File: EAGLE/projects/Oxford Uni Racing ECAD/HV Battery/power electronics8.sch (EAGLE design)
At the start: 65 parts, among them IC1 4043D, IC2 SE555D, IC3 4011D, IC6 4011D, K1 T9AS1D12-48=T9A, K2 T9AS5D12-12=T9A, K3 T9AS1D12-48=T9A, K4 T9AS1D12-48=T9A, K5 T9AS1D12-48=T9A, Q1 BSS138, Q2 BSS138, Q3 BSS138, Q4 BSS138, Q5 BSS138

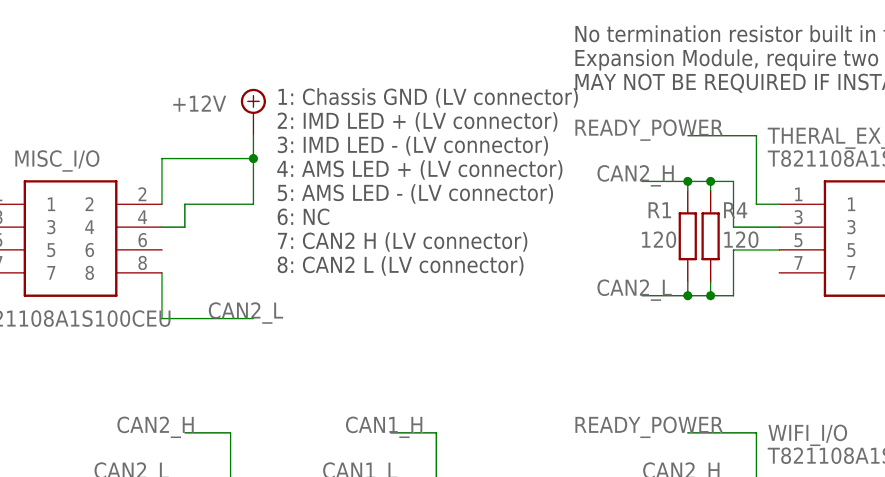
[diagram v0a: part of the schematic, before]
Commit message: connected CAN 1 to misc pcb connector allowing it to be fed to the lv pack connector. This was missing. This has also meant having a single 12V output for both the IMD and AMS warning lights
Signed-off-by: Jack Bruford <jack.bruford41@gmail.com>
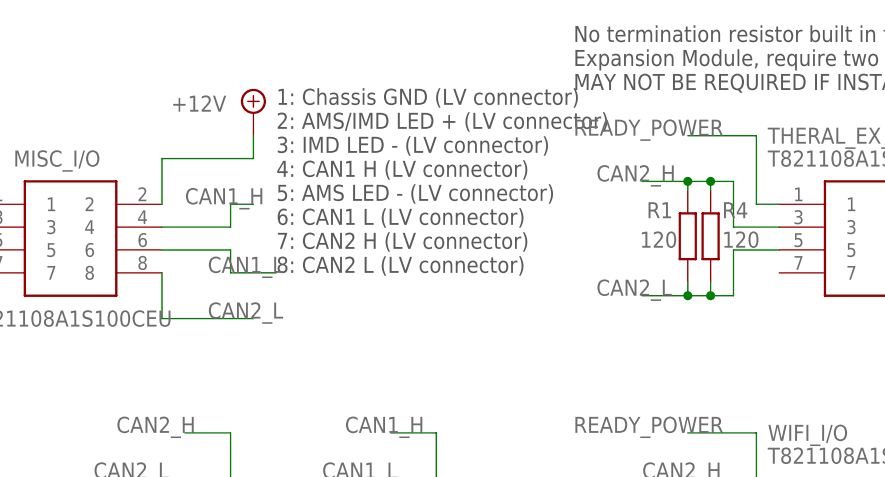
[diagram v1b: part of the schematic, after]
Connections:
- net +12V: no longer MISC_I/O.4
- net CAN1_H: now also MISC_I/O.4
- net CAN1_L: now also MISC_I/O.6
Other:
- note added: "1: Chassis GND (LV connector) 2: AMS/IMD LED + (LV connector) 3: IMD LED - (LV connector) 4: CAN1 H (LV connector) 5: AMS LED - (LV connector) 6: CAN1 L (LV connector) 7: CAN2 H (LV connector) 8: CAN2 L (LV connector)"
- note removed: "1: Chassis GND (LV connector) 2: IMD LED + (LV connector) 3: IMD LED - (LV connector) 4: AMS LED + (LV connector) 5: AMS LED - (LV connector) 6: NC 7: CAN2 H (LV connector) 8: CAN2 L (LV connector)"
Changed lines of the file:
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@@
  a battery voltage source in the application notes</text>
 <text x="170.18" y="152.4" size="1.778" layer="97">1: Chassis GND (LV connector)
-2: IMD LED + (LV connector)
+2: AMS/IMD LED + (LV connector)
 3: IMD LED - (LV connector)
-4: AMS LED + (LV connector)
+4: CAN1 H (LV connector)
 5: AMS LED - (LV connector)
-6: NC
+6: CAN1 L (LV connector)
 7: CAN2 H (LV connector)
 8: CAN2 L (LV connector)</text>
@@
 <pinref part="SUPPLY8" gate="+12V" pin="+12V"/>
 <wire x1="167.64" y1="167.64" x2="167.64" y2="165.1" width="0.1524" layer="91"/>
-<pinref part="MISC_I/O" gate="G$1" pin="4"/>
-<wire x1="157.48" y1="157.48" x2="160.02" y2="157.48" width="0.1524" layer="91"/>
-<wire x1="160.02" y1="157.48" x2="160.02" y2="160.02" width="0.1524" layer="91"/>
-<wire x1="160.02" y1="160.02" x2="167.64" y2="160.02" width="0.1524" layer="91"/>
-<wire x1="167.64" y1="165.1" x2="167.64" y2="160.02" width="0.1524" layer="91"/>
-<junction x="167.64" y="165.1"/>
 </segment>
 </net>
@@
 <label x="30.48" y="139.7" size="1.778" layer="95"/>
 </segment>
+<segment>
+<pinref part="MISC_I/O" gate="G$1" pin="4"/>
+<wire x1="157.48" y1="157.48" x2="165.1" y2="157.48" width="0.1524" layer="91"/>
+<wire x1="165.1" y1="157.48" x2="165.1" y2="160.02" width="0.1524" layer="91"/>
+<wire x1="165.1" y1="160.02" x2="167.64" y2="160.02" width="0.1524" layer="91"/>
+<label x="160.02" y="160.02" size="1.778" layer="95"/>
+</segment>
 </net>
 <net name="CAN1_L" class="0">
@@
 <label x="30.48" y="134.62" size="1.778" layer="95"/>
 </segment>
-</net>
+<segment>
+<pinref part="MISC_I/O" gate="G$1" pin="6"/>
+<wire x1="157.48" y1="154.94" x2="165.1" y2="154.94" width="0.1524" layer="91"/>
+<wire x1="165.1" y1="154.94" x2="165.1" y2="152.4" width="0.1524" layer="91"/>
+<wire x1="165.1" y1="152.4" x2="170.18" y2="152.4" width="0.1524" layer="91"/>
+<label x="162.56" y="152.4" size="1.778" layer="95"/>
+</segment>
+</net>

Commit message: changes before laptop dies
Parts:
- added TP10, TP11, TP12: TPSTP11R, testpad:TPSTP11R
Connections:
- net OK_HS: now also TP10.PP
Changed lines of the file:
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@@
 <part name="Q5" library="m-pad-2.1" deviceset="BSS138" device=""/>
 <part name="IC3" library="40xx" library_urn="urn:adsk.eagle:library:80" deviceset="4011" device="D" package3d_urn="urn:adsk.eagle:package:823/2"/>
+<part name="TP10" library="testpad" library_urn="urn:adsk.eagle:library:385" deviceset="TPS" device="TP11R" package3d_urn="urn:adsk.eagle:package:27961/1" value="TPSTP11R"/>
+<part name="TP11" library="testpad" library_urn="urn:adsk.eagle:library:385" deviceset="TPS" device="TP11R" package3d_urn="urn:adsk.eagle:package:27961/1" value="TPSTP11R"/>
+<part name="TP12" library="testpad" library_urn="urn:adsk.eagle:library:385" deviceset="TPS" device="TP11R" package3d_urn="urn:adsk.eagle:package:27961/1" value="TPSTP11R"/>
 </parts>
 <sheets>
@@
 <attribute name="NAME" x="-54.61" y="37.465" size="1.778" layer="95"/>
 </instance>
+<instance part="TP10" gate="G$1" x="-38.1" y="73.66" smashed="yes">
+<attribute name="NAME" x="-39.37" y="74.93" size="1.778" layer="95"/>
+<attribute name="TP_SIGNAL_NAME" x="-36.83" y="72.39" size="1.778" layer="97"/>
+</instance>
+<instance part="TP11" gate="G$1" x="83.82" y="43.18" smashed="yes">
+<attribute name="NAME" x="82.55" y="44.45" size="1.778" layer="95"/>
+<attribute name="TP_SIGNAL_NAME" x="85.09" y="41.91" size="1.778" layer="97"/>
+</instance>
+<instance part="TP12" gate="G$1" x="83.82" y="35.56" smashed="yes">
+<attribute name="NAME" x="82.55" y="36.83" size="1.778" layer="95"/>
+<attribute name="TP_SIGNAL_NAME" x="85.09" y="34.29" size="1.778" layer="97"/>
+</instance>
 </instances>
 <busses>
@@
 <pinref part="OK2" gate="A" pin="A"/>
 <wire x1="-38.1" y1="68.58" x2="-45.72" y2="68.58" width="0.1524" layer="91"/>
+<pinref part="TP10" gate="G$1" pin="PP"/>
+<wire x1="-38.1" y1="68.58" x2="-38.1" y2="71.12" width="0.1524" layer="91"/>
+<junction x="-38.1" y="68.58"/>
 </segment>
 </net>

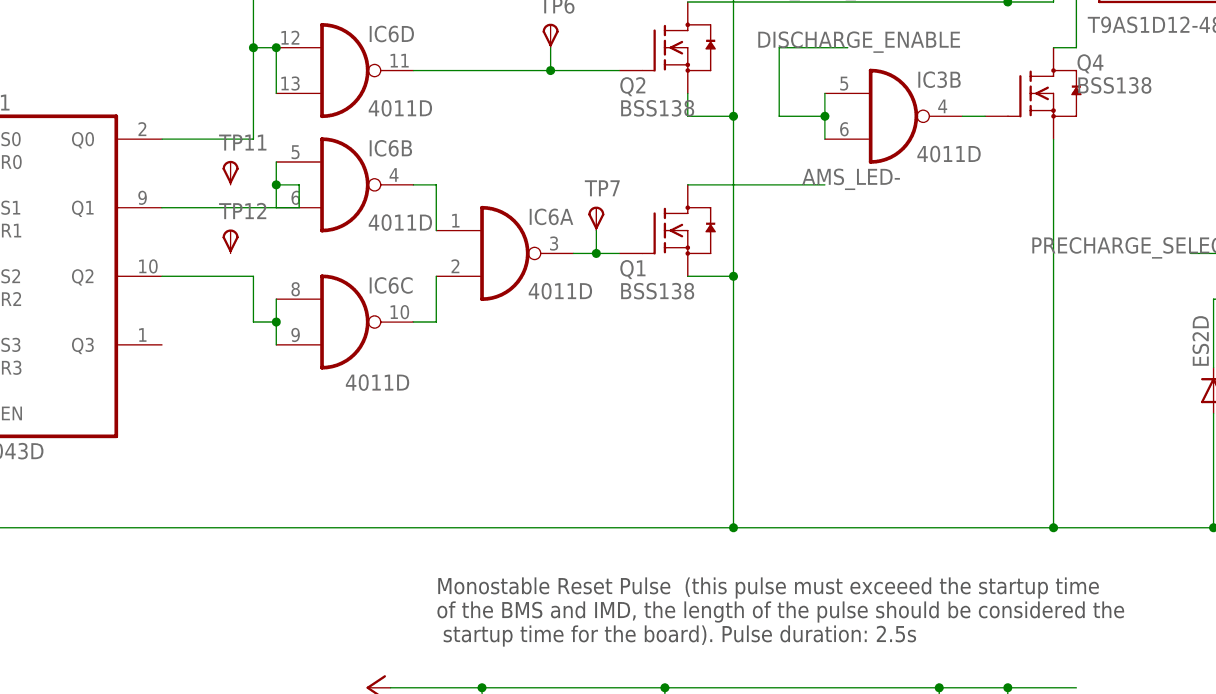
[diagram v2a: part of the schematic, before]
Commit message: Connected TP11 and 12, mods post DRC and ERC, new board layout and rewired CAN to run in parralel
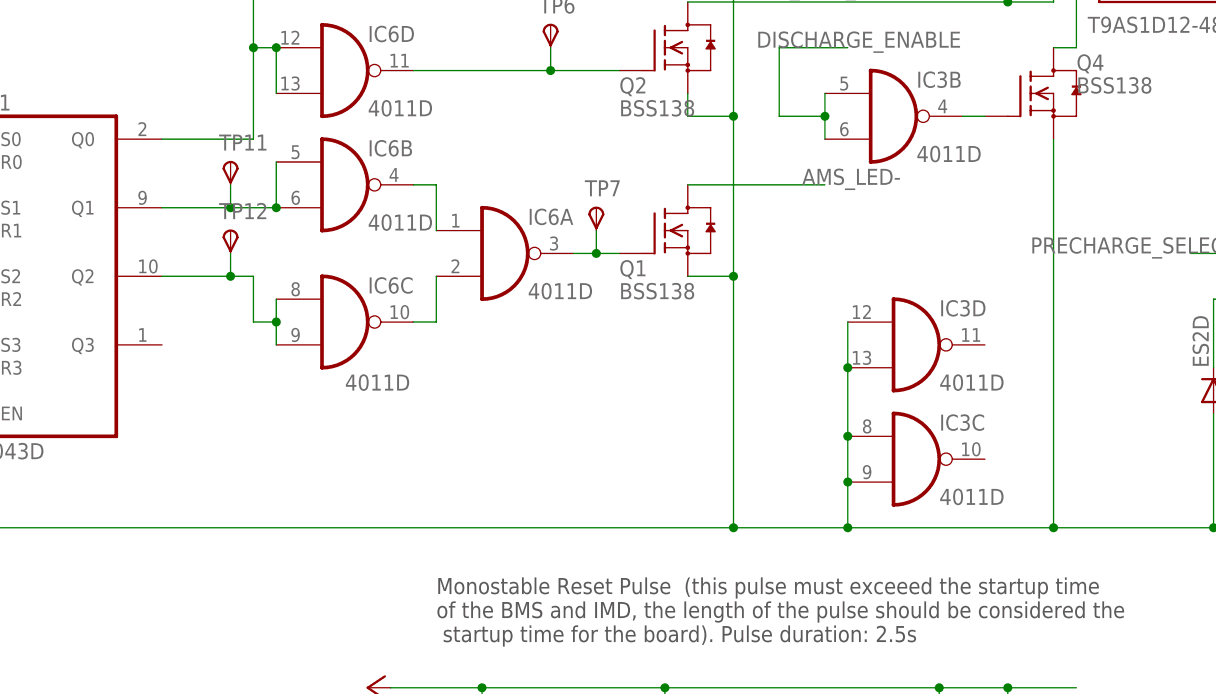
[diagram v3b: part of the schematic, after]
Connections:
- net GND: now also IC3C.I0, IC3C.I1, IC3D.I0, IC3D.I1
- net N$10: now also TP11.PP
- net N$13: now also TP12.PP
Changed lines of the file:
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@@
 <?xml version="1.0" encoding="utf-8"?>
 <!DOCTYPE eagle SYSTEM "eagle.dtd">
-<eagle version="9.2.2">
+<eagle version="9.4.2">
 <drawing>
 <settings>
@@
 <attribute name="TP_SIGNAL_NAME" x="85.09" y="34.29" size="1.778" layer="97"/>
 </instance>
+<instance part="IC3" gate="C" x="160.02" y="10.16" smashed="yes">
+<attribute name="NAME" x="162.56" y="13.335" size="1.778" layer="95"/>
+<attribute name="VALUE" x="162.56" y="5.08" size="1.778" layer="96"/>
+</instance>
+<instance part="IC3" gate="D" x="160.02" y="22.86" smashed="yes">
+<attribute name="NAME" x="162.56" y="26.035" size="1.778" layer="95"/>
+<attribute name="VALUE" x="162.56" y="17.78" size="1.778" layer="96"/>
+</instance>
 </instances>
 <busses>
@@
 <pinref part="IC1" gate="P" pin="VSS"/>
 <wire x1="48.26" y1="2.54" x2="139.7" y2="2.54" width="0.1524" layer="91"/>
-<wire x1="139.7" y1="2.54" x2="175.26" y2="2.54" width="0.1524" layer="91"/>
+<wire x1="139.7" y1="2.54" x2="152.4" y2="2.54" width="0.1524" layer="91"/>
+<wire x1="152.4" y1="2.54" x2="175.26" y2="2.54" width="0.1524" layer="91"/>
 <wire x1="175.26" y1="2.54" x2="193.04" y2="2.54" width="0.1524" layer="91"/>
 <wire x1="-66.04" y1="30.48" x2="-66.04" y2="2.54" width="0.1524" layer="91"/>
@@
 <wire x1="241.3" y1="66.04" x2="241.3" y2="2.54" width="0.1524" layer="91"/>
 <junction x="241.3" y="2.54"/>
+<pinref part="IC3" gate="D" pin="I0"/>
+<pinref part="IC3" gate="D" pin="I1"/>
+<wire x1="152.4" y1="25.4" x2="152.4" y2="20.32" width="0.1524" layer="91"/>
+<pinref part="IC3" gate="C" pin="I0"/>
+<wire x1="152.4" y1="20.32" x2="152.4" y2="12.7" width="0.1524" layer="91"/>
+<junction x="152.4" y="20.32"/>
+<pinref part="IC3" gate="C" pin="I1"/>
+<wire x1="152.4" y1="12.7" x2="152.4" y2="7.62" width="0.1524" layer="91"/>
+<junction x="152.4" y="12.7"/>
+<wire x1="152.4" y1="7.62" x2="152.4" y2="2.54" width="0.1524" layer="91"/>
+<junction x="152.4" y="7.62"/>
+<junction x="152.4" y="2.54"/>
 </segment>
 <segment>
@@
 <segment>
 <pinref part="IC1" gate="A" pin="Q2"/>
-<wire x1="86.36" y1="30.48" x2="76.2" y2="30.48" width="0.1524" layer="91"/>
+<wire x1="86.36" y1="30.48" x2="83.82" y2="30.48" width="0.1524" layer="91"/>
 <pinref part="IC6" gate="C" pin="I0"/>
 <pinref part="IC6" gate="C" pin="I1"/>
+<wire x1="83.82" y1="30.48" x2="76.2" y2="30.48" width="0.1524" layer="91"/>
 <wire x1="88.9" y1="22.86" x2="88.9" y2="25.4" width="0.1524" layer="91"/>
 <wire x1="88.9" y1="25.4" x2="88.9" y2="27.94" width="0.1524" layer="91"/>
@@
 <wire x1="86.36" y1="25.4" x2="88.9" y2="25.4" width="0.1524" layer="91"/>
 <junction x="88.9" y="25.4"/>
+<pinref part="TP12" gate="G$1" pin="PP"/>
+<wire x1="83.82" y1="33.02" x2="83.82" y2="30.48" width="0.1524" layer="91"/>
+<junction x="83.82" y="30.48"/>
 </segment>
 </net>
@@
 <net name="N$10" class="0">
 <segment>
+<pinref part="IC1" gate="A" pin="Q1"/>
+<pinref part="TP11" gate="G$1" pin="PP"/>
+<wire x1="83.82" y1="38.1" x2="76.2" y2="38.1" width="0.1524" layer="91"/>
+<wire x1="83.82" y1="40.64" x2="83.82" y2="38.1" width="0.1524" layer="91"/>
 <pinref part="IC6" gate="B" pin="I1"/>
+<wire x1="83.82" y1="38.1" x2="88.9" y2="38.1" width="0.1524" layer="91"/>
+<junction x="83.82" y="38.1"/>
 <pinref part="IC6" gate="B" pin="I0"/>
-<wire x1="88.9" y1="43.18" x2="88.9" y2="40.64" width="0.1524" layer="91"/>
-<wire x1="88.9" y1="40.64" x2="88.9" y2="38.1" width="0.1524" layer="91"/>
-<wire x1="88.9" y1="40.64" x2="91.44" y2="40.64" width="0.1524" layer="91"/>
-<wire x1="91.44" y1="40.64" x2="91.44" y2="38.1" width="0.1524" layer="91"/>
-<junction x="88.9" y="40.64"/>
-<pinref part="IC1" gate="A" pin="Q1"/>
-<wire x1="91.44" y1="38.1" x2="76.2" y2="38.1" width="0.1524" layer="91"/>
+<wire x1="88.9" y1="38.1" x2="88.9" y2="43.18" width="0.1524" layer="91"/>
+<junction x="88.9" y="38.1"/>
 </segment>
 </net>
@@
 </sheet>
 </sheets>
+<errors>
+</errors>
 </schematic>
 </drawing>

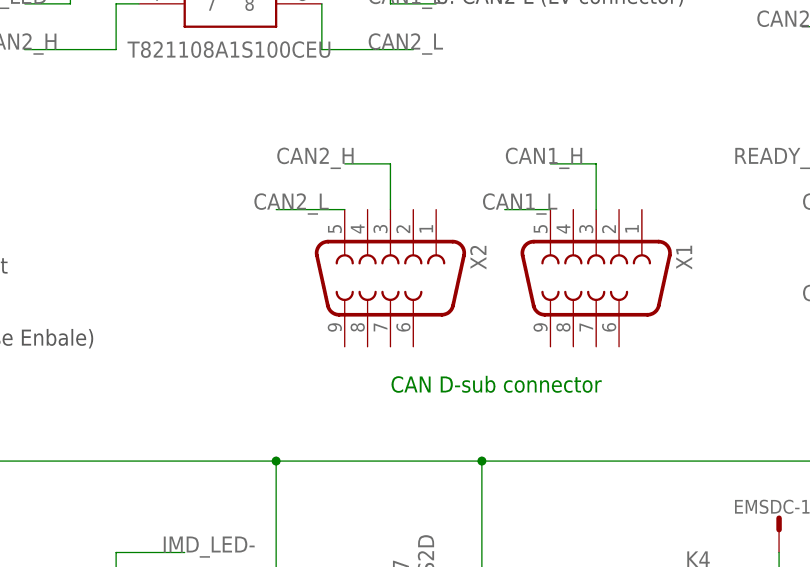
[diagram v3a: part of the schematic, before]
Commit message: Made edits as suggested by William Matthews and generated Gerber files
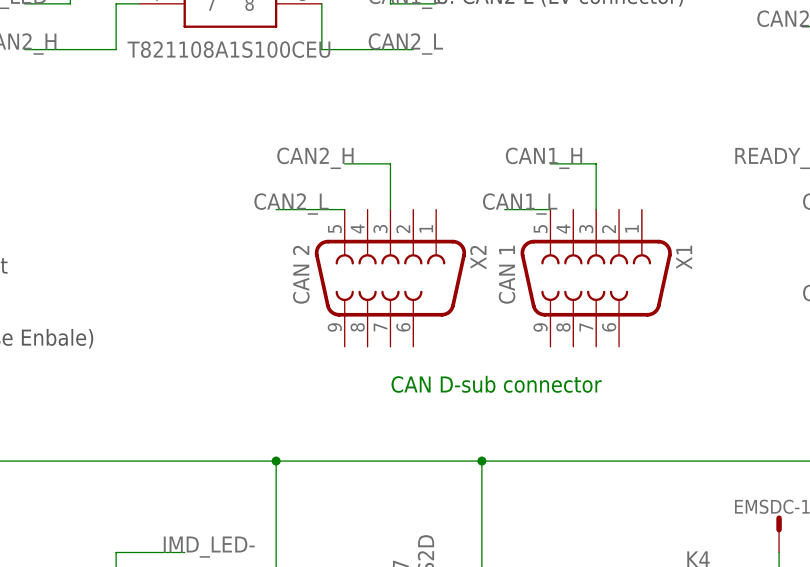
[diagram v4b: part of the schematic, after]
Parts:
- X1: value (none) -> CAN 1
- X2: value (none) -> CAN 2
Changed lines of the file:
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@@
 <?xml version="1.0" encoding="utf-8"?>
 <!DOCTYPE eagle SYSTEM "eagle.dtd">
-<eagle version="9.4.2">
+<eagle version="9.2.2">
 <drawing>
 <settings>
@@
 <part name="TP8" library="testpad" library_urn="urn:adsk.eagle:library:385" deviceset="TPS" device="TP11R" package3d_urn="urn:adsk.eagle:package:27961/1" value="TPSTP11R"/>
 <part name="TP9" library="testpad" library_urn="urn:adsk.eagle:library:385" deviceset="TPS" device="TP11R" package3d_urn="urn:adsk.eagle:package:27961/1" value="TPSTP11R"/>
-<part name="X1" library="con-subd" library_urn="urn:adsk.eagle:library:189" deviceset="F09" device="V" package3d_urn="urn:adsk.eagle:package:10277/1"/>
-<part name="X2" library="con-subd" library_urn="urn:adsk.eagle:library:189" deviceset="F09" device="V" package3d_urn="urn:adsk.eagle:package:10277/1"/>
+<part name="X1" library="con-subd" library_urn="urn:adsk.eagle:library:189" deviceset="F09" device="V" package3d_urn="urn:adsk.eagle:package:10277/1" value="CAN 1"/>
+<part name="X2" library="con-subd" library_urn="urn:adsk.eagle:library:189" deviceset="F09" device="V" package3d_urn="urn:adsk.eagle:package:10277/1" value="CAN 2"/>
 <part name="BMS_POWER/GND" library="con-molex" library_urn="urn:adsk.eagle:library:165" deviceset="KK-156-3" device=""/>
 <part name="OK2" library="optocoupler" library_urn="urn:adsk.eagle:library:320" deviceset="HCPL0453" device="" package3d_urn="urn:adsk.eagle:package:21945/1"/>
